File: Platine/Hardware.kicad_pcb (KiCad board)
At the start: 2 copper layers, 245 x 250 mm, 171 parts, among them J1 Barrel_Jack_Switch, J2 Screw_Terminal_01x02, J3 USB_B, Q1 BCX19, Q2 BCX19, Q3 DMP3098L7, SW1 SW_Soft_Reset, SW2 SW_Hard_Reset, SW3 SW_Flash, SW4 SW_DPDT_x2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

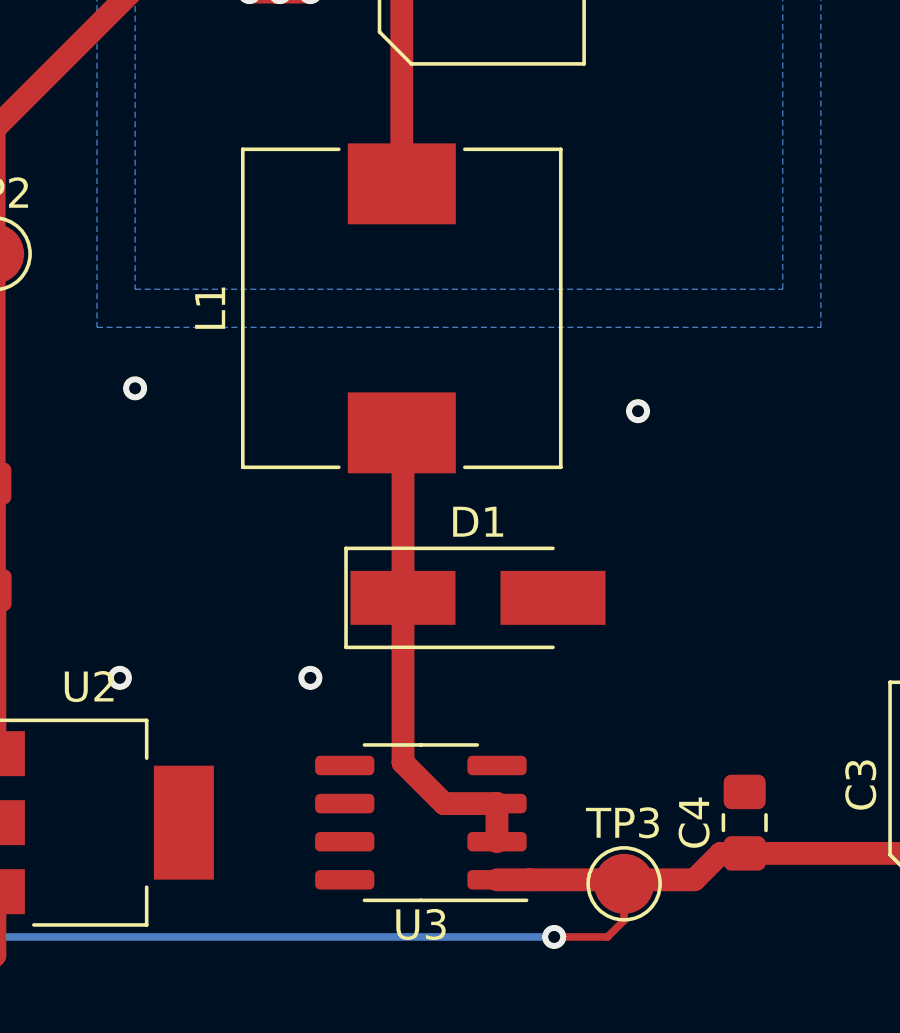
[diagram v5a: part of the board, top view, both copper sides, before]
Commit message: Rerouted feedbackline. close #4 Rerouted to after smoothing coil
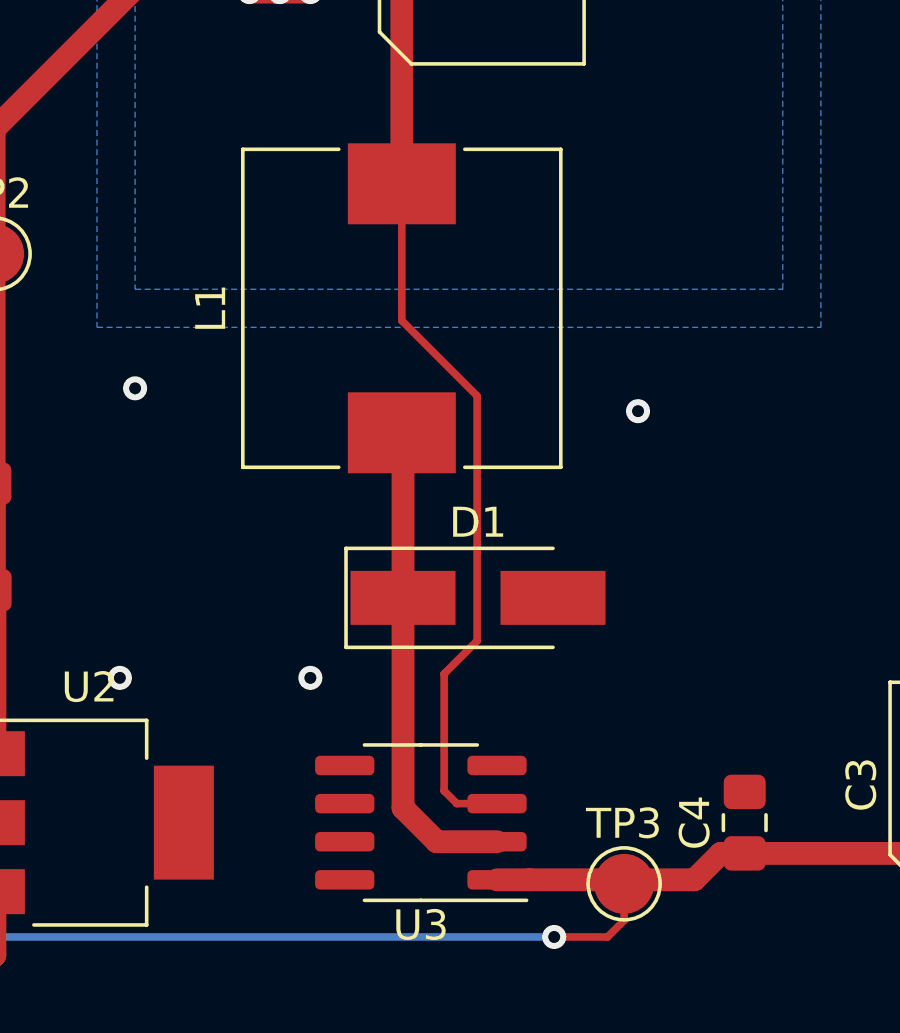
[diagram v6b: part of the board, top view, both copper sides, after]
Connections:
- U3 pad 3: Net-(D1-Pad1) -> VCC
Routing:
- net VCC: track 295.3 -> 319.0 mm
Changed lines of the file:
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@@
     (thickness 1.6)
     (drawings 34)
-    (tracks 901)
+    (tracks 906)
     (zones 0)
     (modules 171)
@@
   )
   (setup
-    (last_trace_width 0.762)
+    (last_trace_width 0.254)
     (user_trace_width 0.2286)
     (user_trace_width 0.254)
@@
       (net 1 GND))
     (pad 3 smd roundrect (at -2.5375 0.635 180) (size 1.975 0.65) (layers F.Cu F.Paste F.Mask) (roundrect_rratio 0.25)
-      (net 45 "Net-(D1-Pad1)"))
+      (net 189 VCC))
     (pad 2 smd roundrect (at -2.5375 -0.635 180) (size 1.975 0.65) (layers F.Cu F.Paste F.Mask) (roundrect_rratio 0.25)
       (net 45 "Net-(D1-Pad1)"))
@@
   (segment (start 245.119 37.919) (end 245.05 37.85) (width 0.381) (layer F.Cu) (net 44))
   (segment (start 245.119 41.91) (end 245.119 37.919) (width 0.381) (layer F.Cu) (net 44))
-  (segment (start 215.2625 252.095) (end 215.2625 250.825) (width 0.762) (layer F.Cu) (net 45))
-  (segment (start 212.13 245.629) (end 212.13 243.967) (width 0.762) (layer F.Cu) (net 45))
-  (segment (start 212.13 249.458516) (end 212.13 245.629) (width 0.762) (layer F.Cu) (net 45))
-  (segment (start 213.496484 250.825) (end 212.13 249.458516) (width 0.762) (layer F.Cu) (net 45))
-  (segment (start 215.2625 250.825) (end 213.496484 250.825) (width 0.762) (layer F.Cu) (net 45))
   (segment (start 212.13 238.505) (end 212.09 238.465) (width 0.762) (layer F.Cu) (net 45))
   (segment (start 212.13 243.967) (end 212.13 238.505) (width 0.762) (layer F.Cu) (net 45))
+  (segment (start 212.13 243.967) (end 212.13 250.97) (width 0.762) (layer F.Cu) (net 45))
+  (segment (start 213.255 252.095) (end 215.2625 252.095) (width 0.762) (layer F.Cu) (net 45))
+  (segment (start 212.13 250.97) (end 213.255 252.095) (width 0.762) (layer F.Cu) (net 45))
   (segment (start 36.054 197.15) (end 35.05 197.15) (width 0.254) (layer F.Cu) (net 46))
   (segment (start 36.881001 196.322999) (end 36.054 197.15) (width 0.254) (layer F.Cu) (net 46))
@@
   (segment (start 185.166 222.684) (end 185.166 221.472) (width 0.762) (layer F.Cu) (net 189))
   (segment (start 204.089 222.758) (end 185.24 222.758) (width 0.762) (layer F.Cu) (net 189))
+  (segment (start 214.6 237.236398) (end 212.09 234.726398) (width 0.254) (layer F.Cu) (net 189))
+  (segment (start 212.09 234.726398) (end 212.09 230.165) (width 0.254) (layer F.Cu) (net 189))
+  (segment (start 213.925 250.825) (end 213.5 250.4) (width 0.254) (layer F.Cu) (net 189))
+  (segment (start 214.6 245.4) (end 214.6 237.236398) (width 0.254) (layer F.Cu) (net 189))
+  (segment (start 215.2625 250.825) (end 213.925 250.825) (width 0.254) (layer F.Cu) (net 189))
+  (segment (start 213.5 246.5) (end 214.6 245.4) (width 0.254) (layer F.Cu) (net 189))
+  (segment (start 213.5 250.4) (end 213.5 246.5) (width 0.254) (layer F.Cu) (net 189))
   (segment (start 250.825 252.73) (end 242.61 252.73) (width 0.762) (layer F.Cu) (net 190))
   (segment (start 242.57 252.69) (end 231.975 252.69) (width 0.762) (layer F.Cu) (net 190))

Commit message: Added Info to silkscreen Polarity info added. close #10, close #3 Added ESD warning Changed revision marker to V1.1 Added switch labeling
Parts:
- added REF**: ESD-Logo_13.2x12mm_SilkScreen, Symbol:ESD-Logo_13.2x12mm_SilkScreen, F.Cu at (59.4, 229.5)
- added REF**: Polarity_Center_Positive_6mm_SilkScreen, Symbol:Polarity_Center_Positive_6mm_SilkScreen, F.Cu at (234.7, 240.0)
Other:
- board text added: "+ -"
- board text added: "Designed by Linda Heinrich & Mathis Lehmann Version 1.1 PSP2020 © Siemens Mobility GmbH"
- board text added: "Electrostatic-sensitive device"
- board text added: "Run Flash / Debug"
- board text added: "V input: 7 - 28 V A max: 2 A"
- board text removed: "Designed by Linda Heinrich & Mathis Lehmann Version 1.0 PSP2020 © Siemens Mobility GmbH"
- board text removed: "V input: 6 - 28 V A max: 2 A"

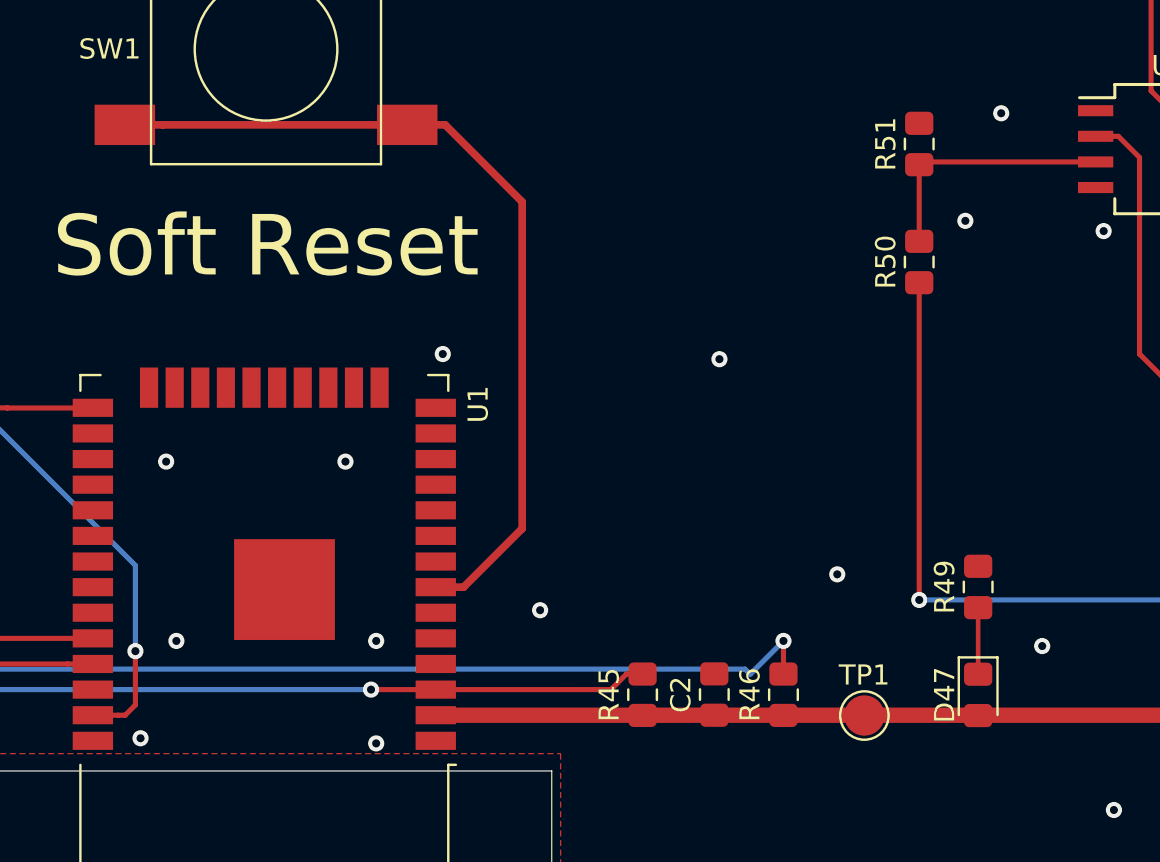
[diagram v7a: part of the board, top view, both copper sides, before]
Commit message: Added Pullup and conneced floating GND peninsulas Added 10k pullup on Soft Rest button (close #9) Via'd GND peninsulas to GND to prevent oscillation
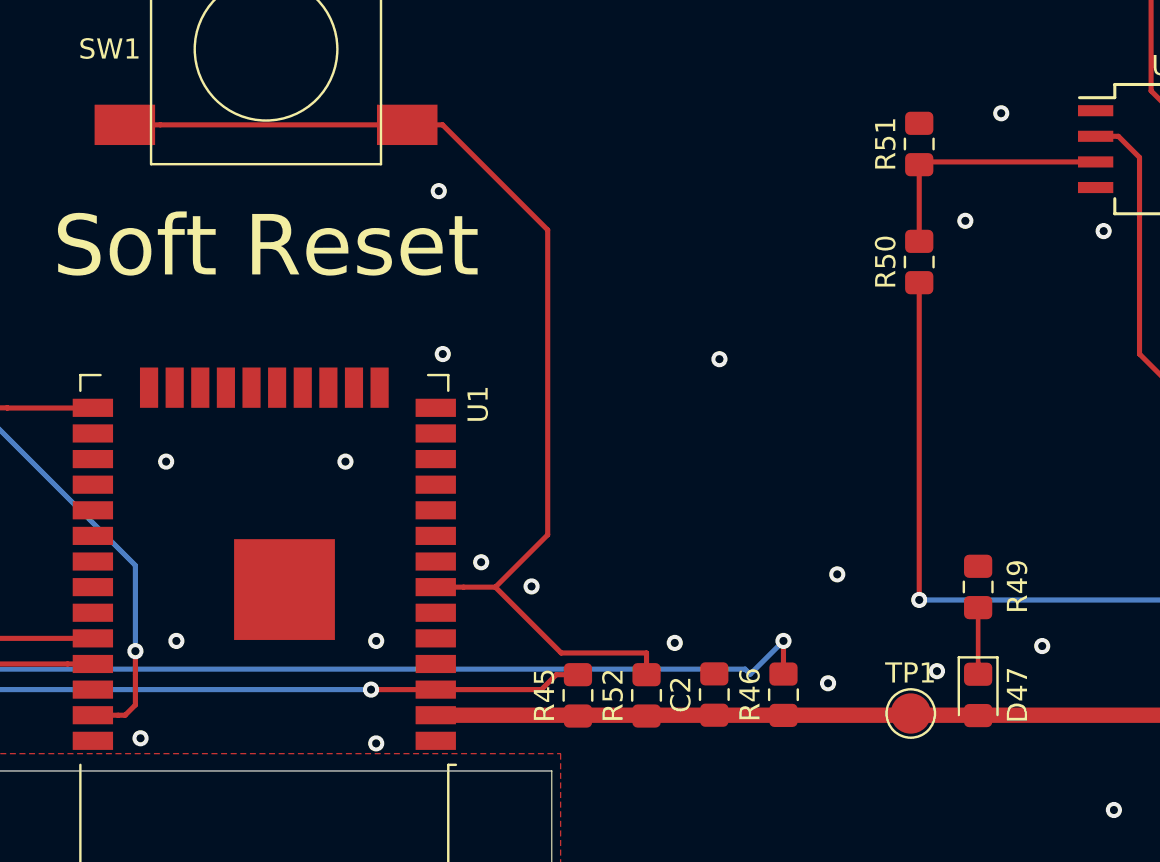
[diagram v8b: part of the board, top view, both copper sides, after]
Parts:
- added R52: 10k, Resistor_SMD:R_0805_2012Metric_Pad1.15x1.40mm_HandSolder, F.Cu at (159.2, 260.0)
- moved R45 3.20 mm to (155.8, 260.0)
- moved TP1 2.30 mm to (172.3, 260.9)
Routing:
- net IO_S_RST: track 43.0 -> 54.8 mm
- net ESP_ENA: track 86.4 -> 83.2 mm
- net GND: vias 65 -> 70
